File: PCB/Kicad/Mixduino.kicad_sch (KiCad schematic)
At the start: 17 parts, among them SW1 BROWSER-L, SW10 SWFX2L, SW11 SWFX1R, SW12 SWFX3L, SW2 BROWSER-R, SW3 SWBR-BACKR, SW4 SWBR-BACKL, SW5 SWBR-PREVR, SW6 SWBR-PREVL, SW7 SWFX2R, SW8 SWFX3R, SW9 SWFX1L

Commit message: PDF
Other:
- sheet NeoPixelsSheet renamed NEOPIXELS
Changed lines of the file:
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@@
   (sheet (at 30.48 144.145) (size 49.53 13.335)
     (stroke (width 0.0006) (type solid) (color 0 0 0 0))
-    (fill (color 72 72 72 0.0000))
-    (property "Sheet name" "NeoPixelsSheet" (id 0) (at 30.48 143.5093 0)
+    (fill (color 0 0 0 0.0000))
+    (property "Sheet name" "NEOPIXELS" (id 0) (at 30.48 143.5093 0)
       (effects (font (size 1.27 1.27)) (justify left bottom))
     )
@@
   (sheet (at 30.48 74.295) (size 49.53 13.335)
     (stroke (width 0) (type solid) (color 0 0 0 0))
-    (fill (color 72 72 72 0.0000))
+    (fill (color 0 0 0 0.0000))
     (property "Sheet name" "TOP POTS" (id 0) (at 30.48 73.7865 0)
       (effects (font (size 1.016 1.016)) (justify left bottom))
@@
     (path "/27ec6e33-6a27-4865-8f8e-aab38be2398e" (page "7"))
     (path "/e43e7bae-0787-4a3c-8ec7-ad7b58132d1f" (page "12"))
-    (path "/00000000-0000-0000-0000-000060683d75/d54ed4a7-12c1-43b6-aca6-0c0808e5cb0b" (page ""))
-    (path "/00000000-0000-0000-0000-000060683d75/352f359b-1f4d-4aa1-988c-1006e0038989" (page ""))
-    (path "/00000000-0000-0000-0000-000060683d75/7e6c461e-b153-4f89-9fb9-2d3cd238f913" (page ""))
-    (path "/00000000-0000-0000-0000-000060683d75/2bcf8ad1-ee6c-4efe-8bf4-67e1c2aaad43" (page ""))
-    (path "/00000000-0000-0000-0000-000060683d75/52615418-7e59-480e-bc5e-b4080c51c540" (page ""))
+    (path "/00000000-0000-0000-0000-000060683d75/d54ed4a7-12c1-43b6-aca6-0c0808e5cb0b" (page "#"))
+    (path "/00000000-0000-0000-0000-000060683d75/352f359b-1f4d-4aa1-988c-1006e0038989" (page "#"))
+    (path "/00000000-0000-0000-0000-000060683d75/7e6c461e-b153-4f89-9fb9-2d3cd238f913" (page "#"))
+    (path "/00000000-0000-0000-0000-000060683d75/2bcf8ad1-ee6c-4efe-8bf4-67e1c2aaad43" (page "#"))
+    (path "/00000000-0000-0000-0000-000060683d75/52615418-7e59-480e-bc5e-b4080c51c540" (page "#"))
   )
   (symbol_instances

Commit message: routing WIP
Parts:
- SW10, SW11, SW12, SW3, SW4, SW5, SW6, SW7, SW8, SW9: footprint Library:SW_PUSH_6mm_H8mm -> Library:SW_Push_1P1T_NO_6x6mm_H8mm
- TB1, TB2: footprint Library:trillbar -> Library:JST_XHP_XH-A-1_1x04_P2.54mm_Horizontal
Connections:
- net FB-L-LATCH: now also XA1.D37; no longer XA1.D39
- net FB-L-SIG: now also XA1.D39; no longer XA1.D37
- net FB-R-LATCH: now also XA1.D42; no longer XA1.D44
- net FB-R-SIG: now also XA1.D44; no longer XA1.D42

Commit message: routes done
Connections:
- net at XA1.D11: now also SW12.2; no longer SW11.2
- net at XA1.D12: now also SW11.2; no longer SW12.2
- net at SW3.2, XA1.D38: now also SW10.2; no longer SW4.2
- net at XA1.D9: now also SW4.2; no longer SW10.2
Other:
- moved on the sheet: SW10, SW11, SW12, SW4
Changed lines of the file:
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@@
   (symbol (lib_id "mixduino-mk2:SW_Push") (at 227.965 102.235 0) (mirror y) (unit 1)
     (in_bom yes) (on_board yes)
-    (property "Reference" "SW4" (id 0) (at 233.045 99.695 0)
+    (property "Reference" "SW10" (id 0) (at 233.045 99.695 0)
       (effects (font (size 1.27 1.27)) (justify left))
     )
-    (property "Value" "SWBR-BACKL" (id 1) (at 222.885 99.695 0))
+    (property "Value" "SWFX2L" (id 1) (at 222.885 99.695 0))
     (property "Footprint" "Library:SW_Push_1P1T_NO_6x6mm_H8mm" (id 2) (at 227.965 97.155 0)
       (effects (font (size 1.27 1.27)) hide)
@@
   (symbol (lib_id "mixduino-mk2:SW_Push") (at 250.19 44.45 0) (mirror y) (unit 1)
     (in_bom yes) (on_board yes)
-    (property "Reference" "SW10" (id 0) (at 255.27 41.91 0)
+    (property "Reference" "SW4" (id 0) (at 255.27 41.91 0)
       (effects (font (size 1.27 1.27)) (justify left))
     )
-    (property "Value" "SWFX2L" (id 1) (at 245.11 41.91 0))
+    (property "Value" "SWBR-BACKL" (id 1) (at 245.11 41.91 0))
     (property "Footprint" "Library:SW_Push_1P1T_NO_6x6mm_H8mm" (id 2) (at 250.19 39.37 0)
       (effects (font (size 1.27 1.27)) hide)
@@
   (symbol (lib_id "mixduino-mk2:SW_Push") (at 250.19 50.8 0) (mirror y) (unit 1)
     (in_bom yes) (on_board yes)
-    (property "Reference" "SW11" (id 0) (at 255.27 48.26 0)
+    (property "Reference" "SW12" (id 0) (at 255.27 48.26 0)
       (effects (font (size 1.27 1.27)) (justify left))
     )
-    (property "Value" "SWFX1R" (id 1) (at 245.11 48.26 0))
+    (property "Value" "SWFX3L" (id 1) (at 245.11 48.26 0))
     (property "Footprint" "Library:SW_Push_1P1T_NO_6x6mm_H8mm" (id 2) (at 250.19 45.72 0)
       (effects (font (size 1.27 1.27)) hide)
@@
   (symbol (lib_id "mixduino-mk2:SW_Push") (at 250.19 57.15 0) (mirror y) (unit 1)
     (in_bom yes) (on_board yes)
-    (property "Reference" "SW12" (id 0) (at 255.27 54.61 0)
+    (property "Reference" "SW11" (id 0) (at 255.27 54.61 0)
       (effects (font (size 1.27 1.27)) (justify left))
     )
-    (property "Value" "SWFX3L" (id 1) (at 245.11 54.61 0))
+    (property "Value" "SWFX1R" (id 1) (at 245.11 54.61 0))
     (property "Footprint" "Library:SW_Push_1P1T_NO_6x6mm_H8mm" (id 2) (at 250.19 52.07 0)
       (effects (font (size 1.27 1.27)) hide)

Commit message: routing WIP
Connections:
- net L2VU-LATCH: now also XA1.D38; no longer XA1.D14 (D14_TX3)
- net L2VU-SIG: now also XA1.D31; no longer XA1.D15 (D15_RX3)
- net R_BROWSER_A: now also XA1.D19 (D19_RX1); no longer XA1.D18 (D18_TX1)
- net R_BROWSER_B: now also XA1.D18 (D18_TX1); no longer XA1.D19 (D19_RX1)
- net at SW5.2, SW6.2: now also XA1.D14 (D14_TX3); no longer XA1.D31
- net at SW4.2: now also SW3.2, XA1.D15 (D15_RX3); no longer XA1.D9
- new net: SW10.2, XA1.D9
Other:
- moved on the sheet: SW10, SW3, SW4, SW5, SW6

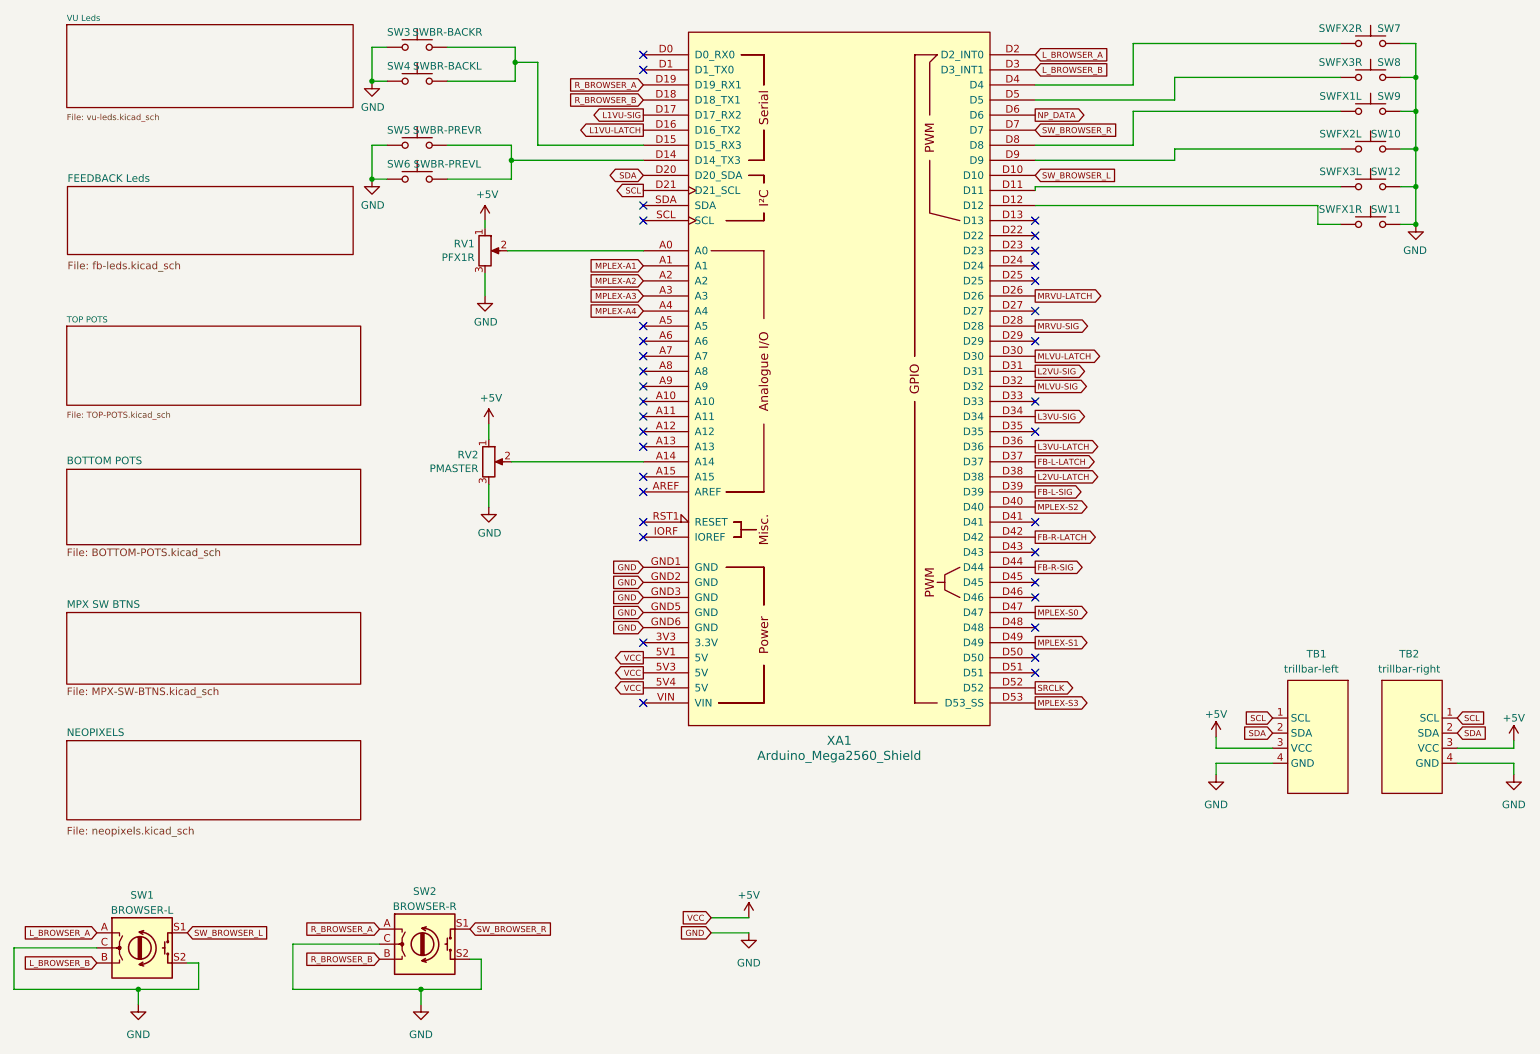
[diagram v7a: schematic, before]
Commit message: update schematic
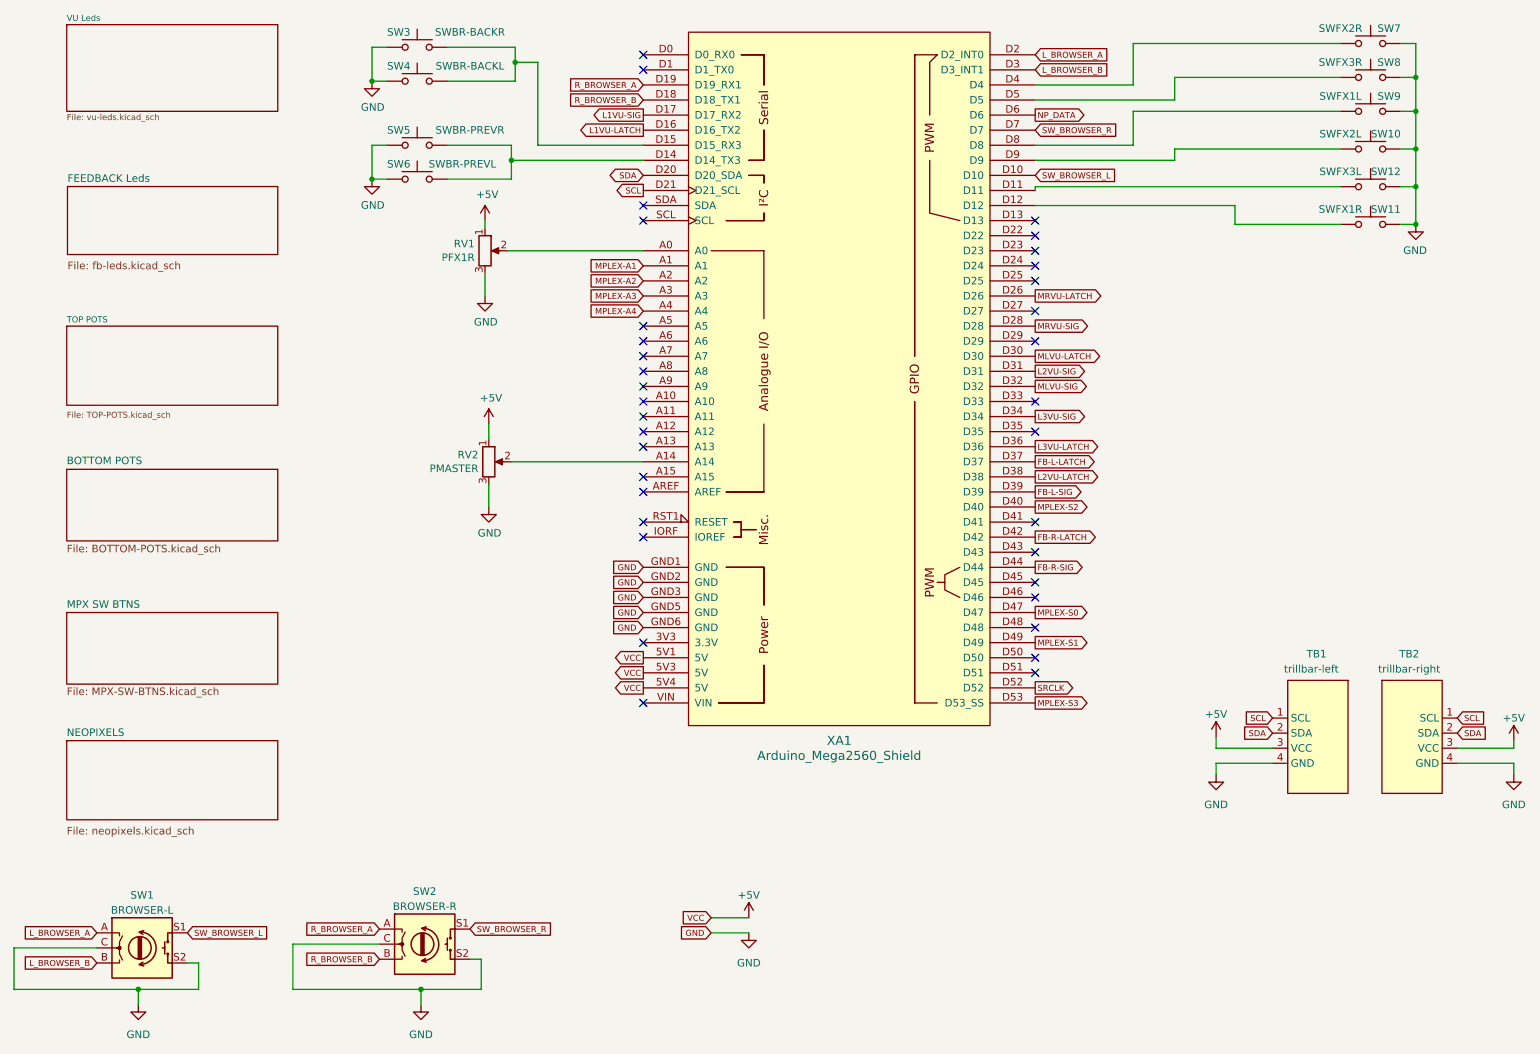
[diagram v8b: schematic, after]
